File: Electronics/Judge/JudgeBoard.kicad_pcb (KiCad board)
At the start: 2 copper layers, 21 parts, among them J1 RJ12-UNSHLD, U1 74HC165, U2 74HC165

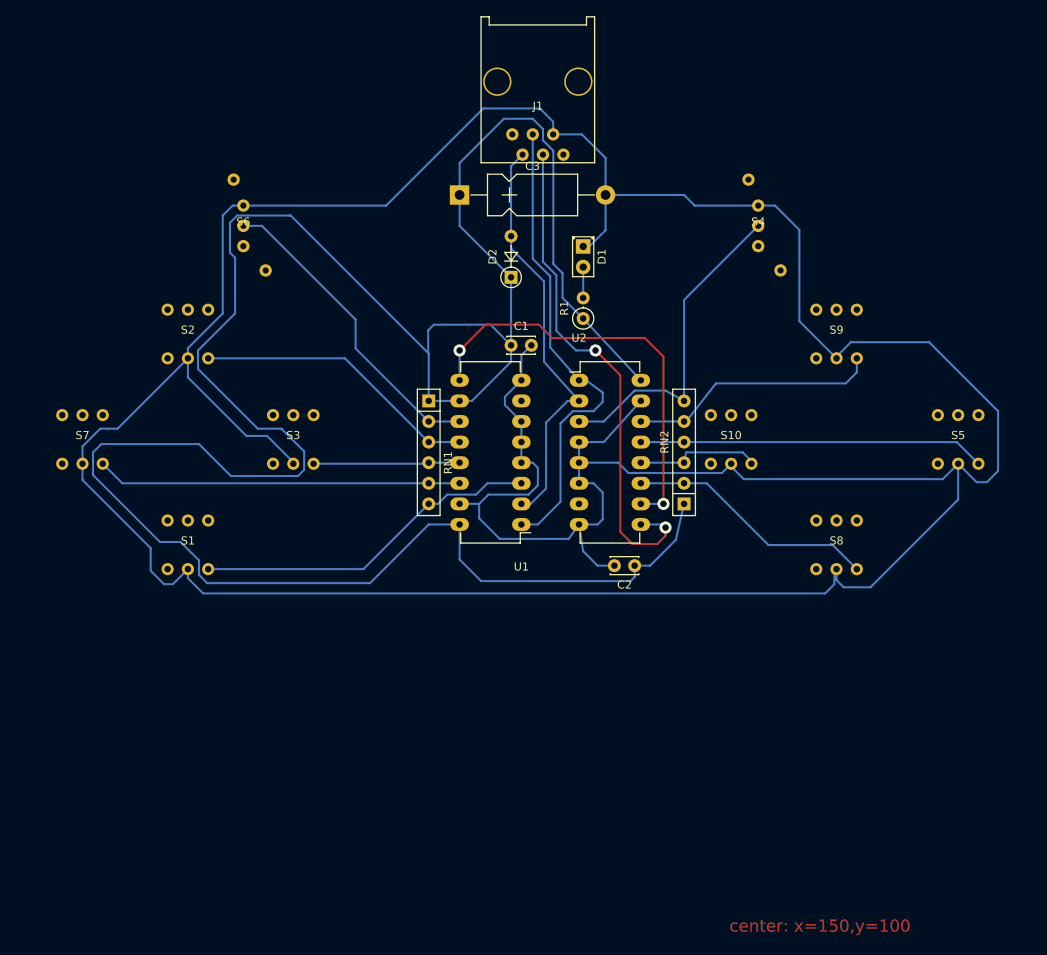
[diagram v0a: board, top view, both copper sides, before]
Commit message: Updated Judge PCB layout to include new footprints
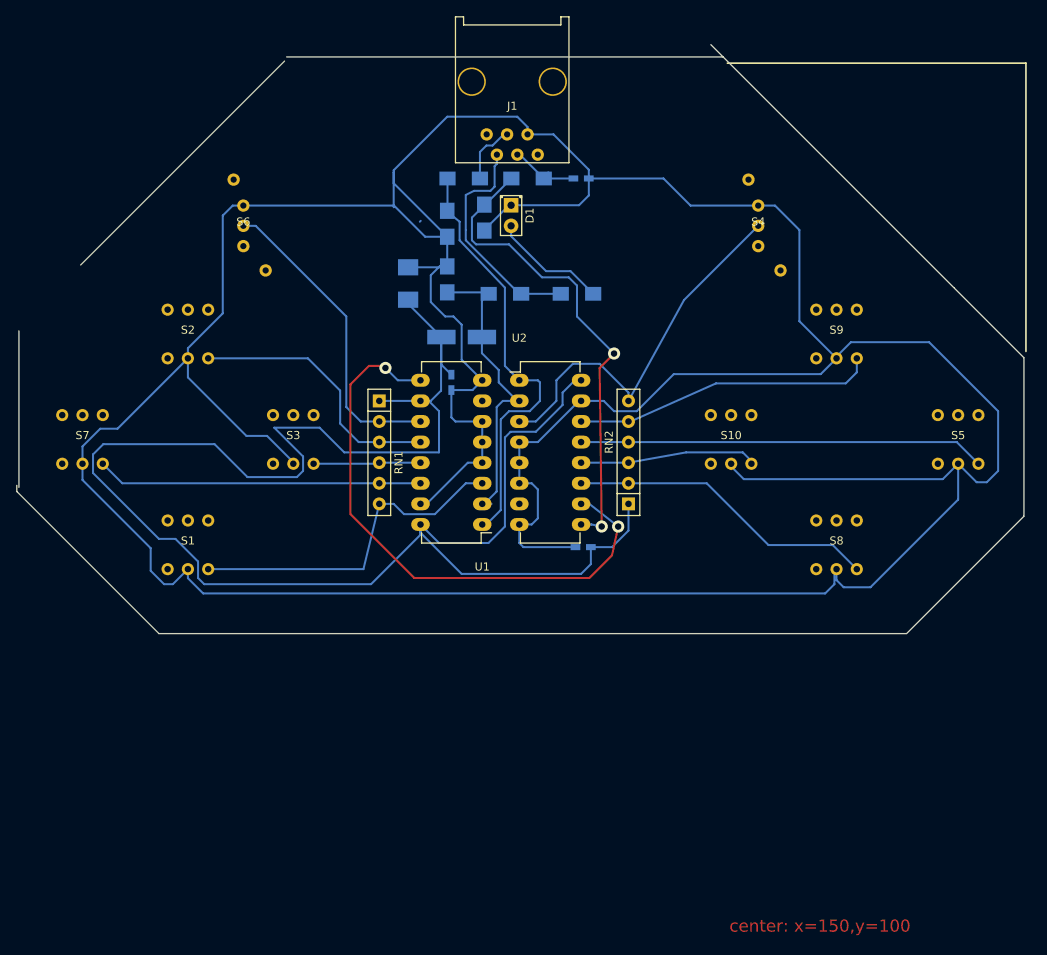
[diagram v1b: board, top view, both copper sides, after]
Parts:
- added C4: 270pF, Capacitors_SMD:C_0603_HandSoldering, B.Cu at (158.5, 67.8)
- added D3: D_Zener, Diodes_SMD:SOD-80C, B.Cu at (142.0, 80.3)
- added D4: D_Zener, Diodes_SMD:SOD-80C, B.Cu at (142.0, 73.4)
- added D5: D_Zener, Diodes_SMD:SOD-80C, B.Cu at (146.6, 72.6)
- added R2: 470, Resistors_SMD:R_1206_HandSoldering, B.Cu at (144.0, 67.8)
- added R3: 470, Resistors_SMD:R_1206_HandSoldering, B.Cu at (151.9, 67.8)
- added R4: 10, Resistors_SMD:R_1206_HandSoldering, B.Cu at (149.1, 82.0)
- C1, C2: value C -> 270pF; footprint Capacitors_THT:C_Disc_D3.4mm_W2.1mm_P2.50mm -> Capacitors_SMD:C_0603_HandSoldering; moved to B.Cu
- C3: value CP1 -> 10uF; footprint Capacitors_THT:CP_Axial_L11.0mm_D5.0mm_P18.00mm_Horizontal -> Capacitors_SMD:C_1210_HandSoldering; moved to B.Cu
- D2: value D -> D_Schottky; footprint Diodes_THT:D_DO-35_SOD27_P5.08mm_Vertical_AnodeUp -> Diodes_SMD:D_SMA_Handsoldering; moved to B.Cu
- R1: value R -> 68; footprint Resistors_THT:R_Axial_DIN0207_L6.3mm_D2.5mm_P2.54mm_Vertical -> Resistors_SMD:R_1206_HandSoldering; moved to B.Cu
- RN1, RN2: value R_Network05 -> 47k
- moved C3 12.6 mm to (137.2, 80.8), turned to 90 degrees
- moved D1 10.2 mm to (149.9, 71.1)
- moved D2 9.56 mm to (143.8, 87.4), turned to 0 degrees
- moved C1 8.67 mm to (142.5, 93.0), turned to 270 degrees
- moved U2 7.37 mm to (150.9, 92.7)
- moved RN2 6.86 mm to (164.3, 108.0)
- moved C2 6.75 mm to (158.8, 113.3)
- moved RN1 6.10 mm to (133.6, 95.2)
- moved U1 4.83 mm to (146.3, 110.5)
- moved J1 3.16 mm to (150.0, 55.9)
- moved R1 3.14 mm to (158.0, 82.0), turned to 180 degrees
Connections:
- J1 pad 2: /CLK -> Net-(J1-Pad2)
- J1 pad 3: /LOAD -> Net-(J1-Pad3)
- J1 pad 4: Net-(J1-Pad4) -> Net-(C4-Pad1)
- R1 pad 1: +3V3 -> Net-(D1-Pad2)
- R1 pad 2: Net-(D1-Pad2) -> Net-(J1-Pad2)
- U2 pad 9: Net-(J1-Pad4) -> Net-(D5-Pad1)
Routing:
- net +3V3: track 305.7 -> 218.6 mm
- net Net-(J1-Pad4): track 62.7 -> 0.00 mm, vias 2 -> 0
- net Net-(D5-Pad1): track 0.00 -> 59.9 mm, vias 0 -> 2
- net GND: track 473.8 -> 524.2 mm
- net Net-(J1-Pad2): track 0.00 -> 29.0 mm
- net Net-(U1-Pad9): track 52.7 -> 72.2 mm
- net Net-(D1-Pad2): track 3.81 -> 14.4 mm
- net /CLK: track 53.1 -> 43.0 mm
- net Net-(C4-Pad1): track 0.00 -> 9.07 mm
- net Net-(J1-Pad3): track 0.00 -> 8.60 mm
- net Net-(RN2-Pad4): track 42.7 -> 50.1 mm
- net Net-(RN2-Pad2): track 31.0 -> 38.4 mm
- net Net-(RN2-Pad6): track 40.2 -> 47.5 mm
- net Net-(RN2-Pad3): track 15.8 -> 22.2 mm
- net Net-(RN2-Pad5): track 31.2 -> 37.3 mm
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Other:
- board outline added: 124.2 x 72.6 mm

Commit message: Updated Judge PCB routing
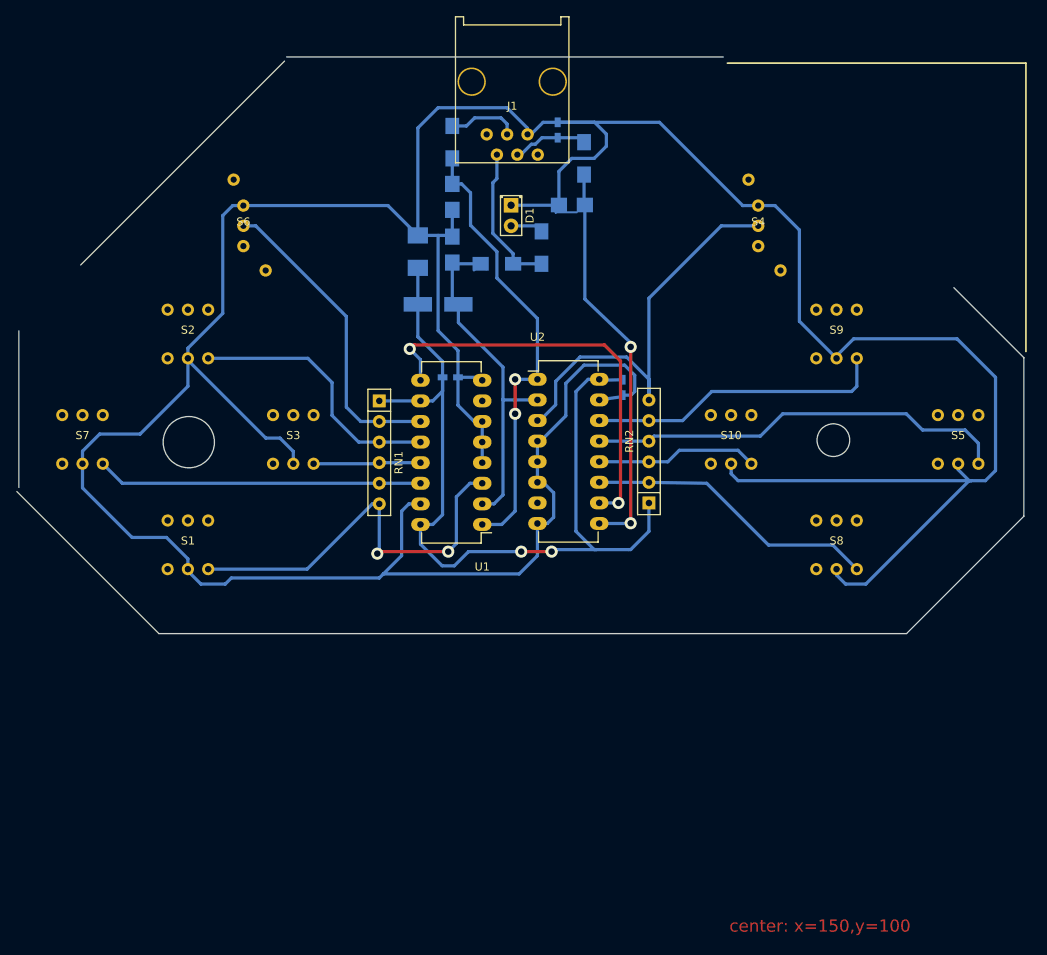
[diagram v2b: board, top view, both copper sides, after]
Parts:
- moved C2 20.3 mm to (163.6, 93.6), turned to 270 degrees
- moved D5 10.9 mm to (157.4, 71.1), turned to 180 degrees
- moved R3 7.40 mm to (158.9, 65.3), turned to 270 degrees
- moved R1 7.19 mm to (153.6, 76.3), turned to 270 degrees
- moved C4 6.64 mm to (155.6, 61.8), turned to 90 degrees
- moved D2 4.97 mm to (140.9, 83.3)
- moved R2 4.69 mm to (142.6, 63.3), turned to 90 degrees
- moved C3 4.11 mm to (138.4, 76.8)
- moved R4 3.83 mm to (148.1, 78.3)
- moved D3 3.73 mm to (142.6, 76.6)
- moved D4 3.37 mm to (142.6, 70.1)
- moved RN2 2.52 mm to (166.9, 107.8)
- moved U2 2.24 mm to (153.1, 92.6)
- moved C1 0.64 mm to (142.4, 92.3), turned to 0 degrees
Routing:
- net +3V3: track 218.6 -> 113.9 mm, vias 0 -> 2
- net GND: track 524.2 -> 463.5 mm
- net Net-(U1-Pad9): track 72.2 -> 52.5 mm
- net Net-(D5-Pad1): track 59.9 -> 49.3 mm
- net Net-(D1-Pad2): track 14.4 -> 4.03 mm
- net Net-(J1-Pad2): track 29.0 -> 19.5 mm
- net /CLK: track 43.0 -> 50.8 mm
- net Net-(RN1-Pad6): track 42.9 -> 50.6 mm, vias 0 -> 2
- net Net-(RN2-Pad6): track 47.5 -> 52.5 mm
- net /LOAD: track 54.4 -> 58.0 mm, vias 0 -> 2
- net Net-(RN2-Pad2): track 38.4 -> 36.2 mm
- net Net-(RN2-Pad4): track 50.1 -> 52.2 mm
- net Net-(RN2-Pad3): track 22.2 -> 20.4 mm
- net Net-(C4-Pad1): track 9.07 -> 10.6 mm
- net Net-(J1-Pad3): track 8.60 -> 9.19 mm
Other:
- board size 124.2 x 72.6 mm -> 124.2 x 71.1 mm
- net class Default: clearance 0.2 -> 0.3; trace_width 0.25 -> 0.4
- rule trace_clearance: 0.2 -> 0.3

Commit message: Updated Judge PCB for manufacturability
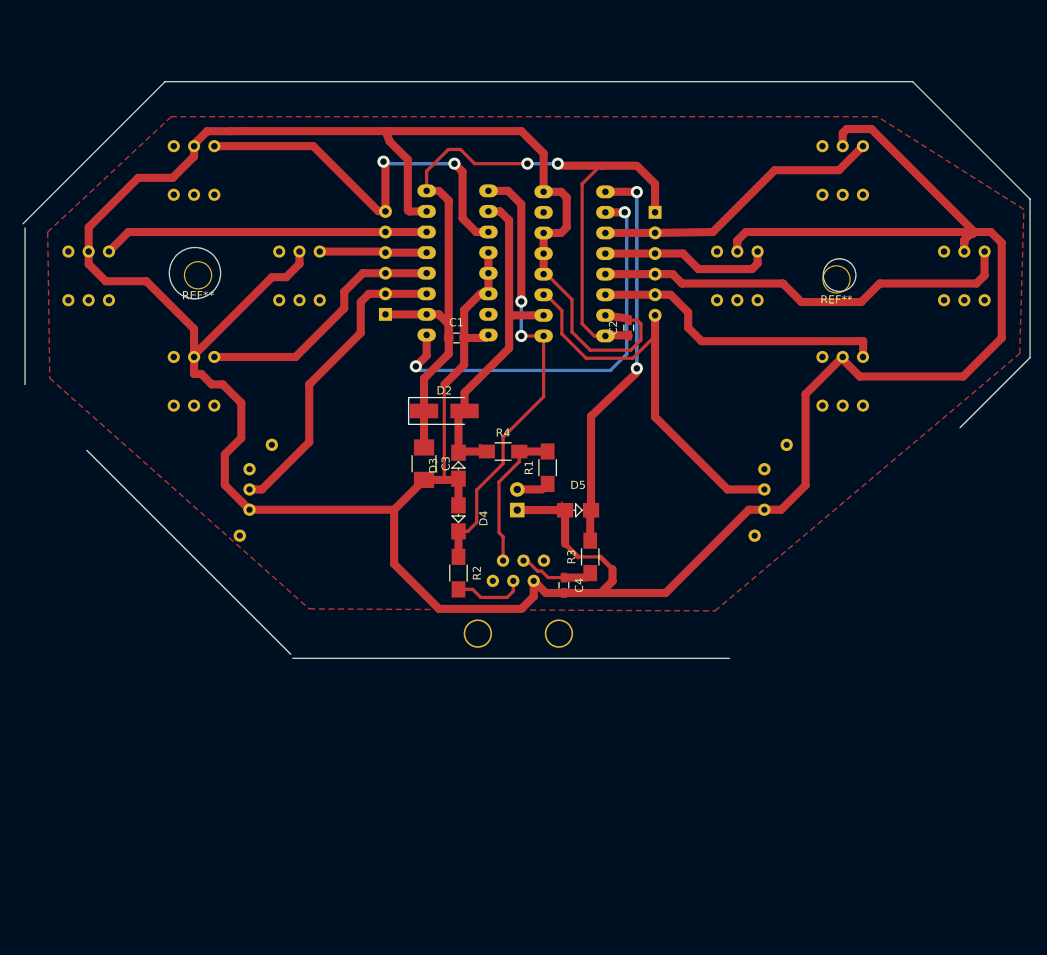
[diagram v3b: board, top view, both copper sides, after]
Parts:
- added REF**: M3, Mounting_Holes:M3, F.Cu at (111.3, 79.8)
- added REF**: M3, Mounting_Holes:M3, F.Cu at (190.0, 80.3)
- C1, C2, C3, C4, D2, D3, D4, D5, R1, R2, R3, R4: moved to F.Cu
- D1, J1, RN1, RN2, S1, S10, S2, S3, S4, S5, S6, S7, S8, S9, U1, U2: moved to B.Cu
- moved J1 68.1 mm to (150.8, 124.0)
- moved C4 56.2 mm to (156.4, 118.0), turned to 270 degrees
- moved R2 53.2 mm to (143.4, 116.5), turned to 270 degrees
- moved R3 49.2 mm to (159.6, 114.5), turned to 90 degrees
- moved S1 46.2 mm to (110.8, 66.8)
- moved S8 46.2 mm to (190.8, 66.8)
- moved U1 41.2 mm to (147.1, 69.3)
- moved D4 39.7 mm to (143.4, 109.7), turned to 90 degrees
- moved D5 37.7 mm to (158.1, 108.7)
- moved D1 37.6 mm to (150.6, 108.7), turned to 90 degrees
- moved RN2 35.9 mm to (167.6, 72.0), turned to 270 degrees
- moved S4 32.5 mm to (181.1, 106.2)
- moved S6 32.5 mm to (117.6, 106.2)
- moved R1 27.2 mm to (154.4, 103.5), turned to 90 degrees
- moved D3 26.7 mm to (143.4, 103.2), turned to 270 degrees
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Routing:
- net GND: track 463.5 -> 469.9 mm
- net Net-(RN1-Pad3): track 32.8 -> 31.7 mm
- net Net-(RN2-Pad3): track 20.4 -> 21.3 mm
- added copper zone on F.Cu, net GND
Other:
- outline, holes or cut-outs redrawn
- board text removed: "center: x=150,y=100"

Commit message: Updating judge circuits and pcb to match timer
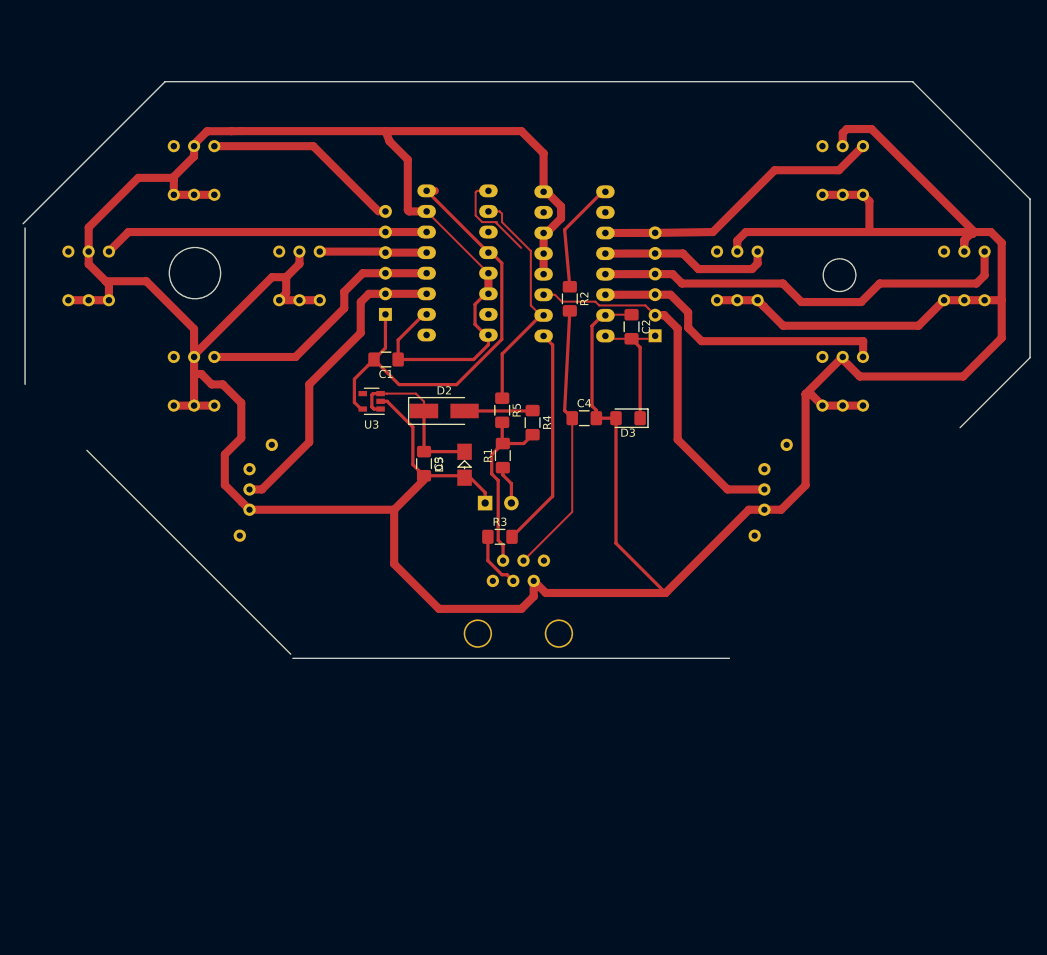
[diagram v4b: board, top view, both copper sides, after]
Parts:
- removed D4: D_Zener, Diodes_SMD:SOD-80C
- removed REF** (x2): M3, Mounting_Holes:M3
- added R5: 470, Resistor_SMD:R_1206_3216Metric_Pad1.42x1.75mm_HandSolder, F.Cu at (148.8, 96.4)
- added U3: MIC5504-3.3YM5, Package_TO_SOT_SMD:SOT-23-5, F.Cu at (132.7, 95.3)
- C1, C2: value 270pF -> 1uF; footprint Capacitors_SMD:C_0603_HandSoldering -> Capacitor_SMD:C_1206_3216Metric_Pad1.42x1.75mm_HandSolder
- C3: value 10uF -> 1uF; footprint Capacitors_SMD:C_1210_HandSoldering -> Capacitor_SMD:C_1206_3216Metric_Pad1.42x1.75mm_HandSolder
- C4: value 270pF -> 470pF; footprint Capacitors_SMD:C_0603_HandSoldering -> Capacitor_SMD:C_1206_3216Metric_Pad1.42x1.75mm_HandSolder
- D1: footprint LEDs:LED_D2.0mm_W4.8mm_H2.5mm_FlatTop -> LED_THT:LED_D3.0mm_Spread
- D3: value D_Zener -> 3.3V; footprint Diodes_SMD:SOD-80C -> Diode_SMD:D_1206_3216Metric_Pad1.42x1.75mm_HandSolder
- D5: value D_Zener -> 5V
- R1: value 68 -> 470; footprint Resistors_SMD:R_1206_HandSoldering -> Resistor_SMD:R_1206_3216Metric_Pad1.42x1.75mm_HandSolder
- R2: value 470 -> 10; footprint Resistors_SMD:R_1206_HandSoldering -> Resistor_SMD:R_1206_3216Metric_Pad1.42x1.75mm_HandSolder
- R3: footprint Resistors_SMD:R_1206_HandSoldering -> Resistor_SMD:R_1206_3216Metric_Pad1.42x1.75mm_HandSolder
- R4: value 10 -> 100; footprint Resistors_SMD:R_1206_HandSoldering -> Resistor_SMD:R_1206_3216Metric_Pad1.42x1.75mm_HandSolder
- RN1, RN2: footprint Resistors_THT:R_Array_SIP6 -> Resistor_THT:R_Array_SIP6
- moved R2 36.5 mm to (157.1, 82.7)
- moved D3 21.7 mm to (164.3, 97.4), turned to 180 degrees
- moved C4 20.8 mm to (158.9, 97.4), turned to 0 degrees
- moved RN2 15.2 mm to (167.6, 87.2), turned to 90 degrees
- moved D5 15.1 mm to (144.1, 103.1), turned to 270 degrees
- moved R3 11.4 mm to (148.5, 112.0), turned to 0 degrees
- moved C1 9.08 mm to (134.4, 90.1), turned to 180 degrees
- moved R1 5.73 mm to (148.8, 102.0)
- moved R4 5.09 mm to (152.5, 97.9), turned to 270 degrees
- moved D1 3.38 mm to (147.4, 107.8), turned to 0 degrees
- moved C2 0.37 mm to (164.7, 86.1), turned to 270 degrees
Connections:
- net Net-(U1-Pad9) renamed /Q_intermediate
- C1 pad 1: +3V3 -> GND
- C1 pad 2: GND -> +3V3
- C2 pad 1: +3V3 -> GND
- C2 pad 2: GND -> +3V3
- C3 pad 1: +3V3 -> +5V
- D2 pad 1: +3V3 -> +5V
- D2 pad 2: /CLK -> Net-(D2-Pad2)
- D3 pad 1: /CLK -> +3V3
- D5 pad 1: Net-(D5-Pad1) -> +5V
- J1 pad 1: (no net) -> Net-(J1-Pad1)
- J1 pad 6: (no net) -> Net-(J1-Pad6)
- R2 pad 1: /LOAD -> /Q
- R2 pad 2: Net-(J1-Pad3) -> Net-(C4-Pad1)
- R3 pad 1: Net-(C4-Pad1) -> Net-(J1-Pad3)
- R3 pad 2: Net-(D5-Pad1) -> /LOAD
- R4 pad 1: /CLK -> Net-(D2-Pad2)
- S1 pad 3: (no net) -> Net-(S1-Pad3)
- S1 pad 4: (no net) -> GND
- S1 pad 5: (no net) -> GND
- S1 pad 6: (no net) -> GND
- S10 pad 1: Net-(RN2-Pad3) -> Net-(RN2-Pad5)
- S10 pad 3: (no net) -> Net-(S10-Pad3)
- S10 pad 4: (no net) -> GND
- S10 pad 5: (no net) -> GND
- S10 pad 6: (no net) -> GND
- S2 pad 3: (no net) -> Net-(S2-Pad3)
- S2 pad 4: (no net) -> GND
- S2 pad 5: (no net) -> GND
- S2 pad 6: (no net) -> GND
- S3 pad 3: (no net) -> Net-(S3-Pad3)
- S3 pad 4: (no net) -> GND
- S3 pad 5: (no net) -> GND
- S3 pad 6: (no net) -> GND
- S4 pad 1: Net-(RN2-Pad6) -> Net-(RN2-Pad2)
- S4 pad 3: (no net) -> Net-(S4-Pad3)
- S5 pad 3: (no net) -> Net-(S5-Pad3)
- S5 pad 4: (no net) -> GND
- S5 pad 5: (no net) -> GND
- S5 pad 6: (no net) -> GND
- S6 pad 3: (no net) -> Net-(S6-Pad3)
- S7 pad 3: (no net) -> Net-(S7-Pad3)
- S7 pad 4: (no net) -> GND
- S7 pad 5: (no net) -> GND
- S7 pad 6: (no net) -> GND
- S8 pad 1: Net-(RN2-Pad2) -> Net-(RN2-Pad6)
- S8 pad 3: (no net) -> Net-(S8-Pad3)
- S8 pad 4: (no net) -> GND
- S8 pad 5: (no net) -> GND
- S8 pad 6: (no net) -> GND
- S9 pad 1: Net-(RN2-Pad5) -> Net-(RN2-Pad3)
- S9 pad 3: (no net) -> Net-(S9-Pad3)
- S9 pad 4: (no net) -> GND
- S9 pad 5: (no net) -> GND
- S9 pad 6: (no net) -> GND
- U1 pad 10: +3V3 -> GND
- U1 pad 4: GND -> +3V3
- U1 pad 7: (no net) -> Net-(U1-Pad7)
- U2 pad 11: Net-(RN2-Pad2) -> Net-(RN2-Pad6)
- U2 pad 12: Net-(RN2-Pad3) -> Net-(RN2-Pad5)
- U2 pad 14: Net-(RN2-Pad5) -> Net-(RN2-Pad3)
- U2 pad 3: Net-(RN2-Pad6) -> Net-(RN2-Pad2)
- U2 pad 7: (no net) -> Net-(U2-Pad7)
- U2 pad 9: Net-(D5-Pad1) -> /Q
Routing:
- net GND: track 469.9 -> 573.7 mm
- net /Q_intermediate: track 52.5 -> 1.02 mm, vias 2 -> 0
- net Net-(D5-Pad1): track 49.3 -> 0.00 mm, vias 2 -> 0
- net +3V3: track 113.9 -> 74.6 mm, vias 2 -> 0
- net Net-(RN1-Pad6): track 50.6 -> 24.4 mm, vias 2 -> 0
- net Net-(C4-Pad1): track 10.6 -> 34.5 mm
- net +5V: track 0.00 -> 22.2 mm
- net /CLK: track 50.8 -> 32.1 mm
- net /LOAD: track 58.0 -> 40.2 mm, vias 2 -> 0
- net Net-(RN2-Pad6): track 52.5 -> 36.2 mm
- net Net-(RN2-Pad5): track 37.5 -> 21.3 mm
- net Net-(RN2-Pad3): track 21.3 -> 37.5 mm
- net /Q: track 0.00 -> 14.0 mm
- net Net-(RN2-Pad2): track 36.2 -> 45.6 mm
- net Net-(D2-Pad2): track 0.00 -> 8.41 mm
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- removed copper zone on F.Cu, net GND
